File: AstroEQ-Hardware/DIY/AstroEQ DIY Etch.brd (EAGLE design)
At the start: 101.6 x 66 mm, 40 parts, among them IC1 ATMEGA162-16PU, IC2 PIC18F14K50-I/P, IC3 78L05, J1 POWER_JACKPTH, M1 POLOLU-CARRIER, M2 POLOLU-CARRIER, X1 16MHz, X2 12MHz

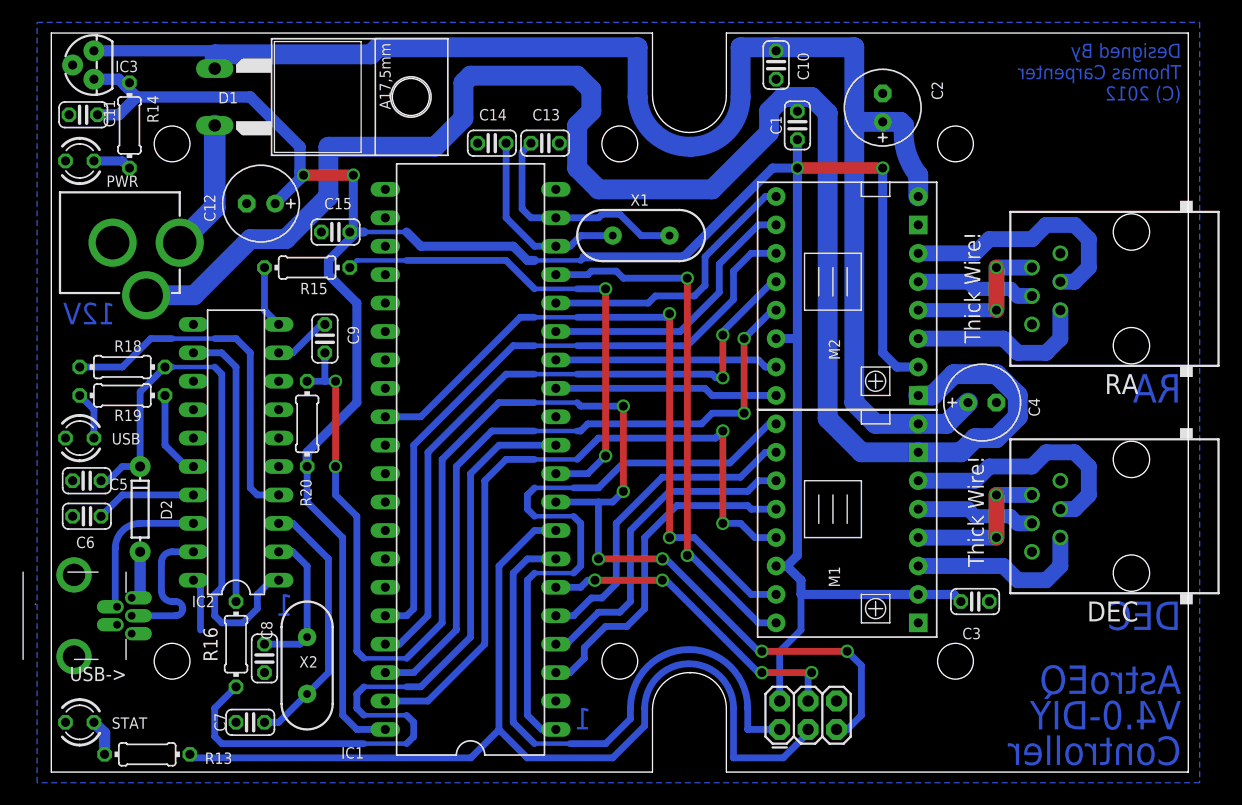
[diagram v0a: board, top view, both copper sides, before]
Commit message: Update DIY Eagle Designs
(1) Bring AstroEQ-DIY up to date (V4.4)
(2) Export AstroEQ-DIY schematic to PDF
(3) Make sure the etch file doesn't have holes in pads
(4) Add AstroEQ-ARD variant - Arduino Mega sheild
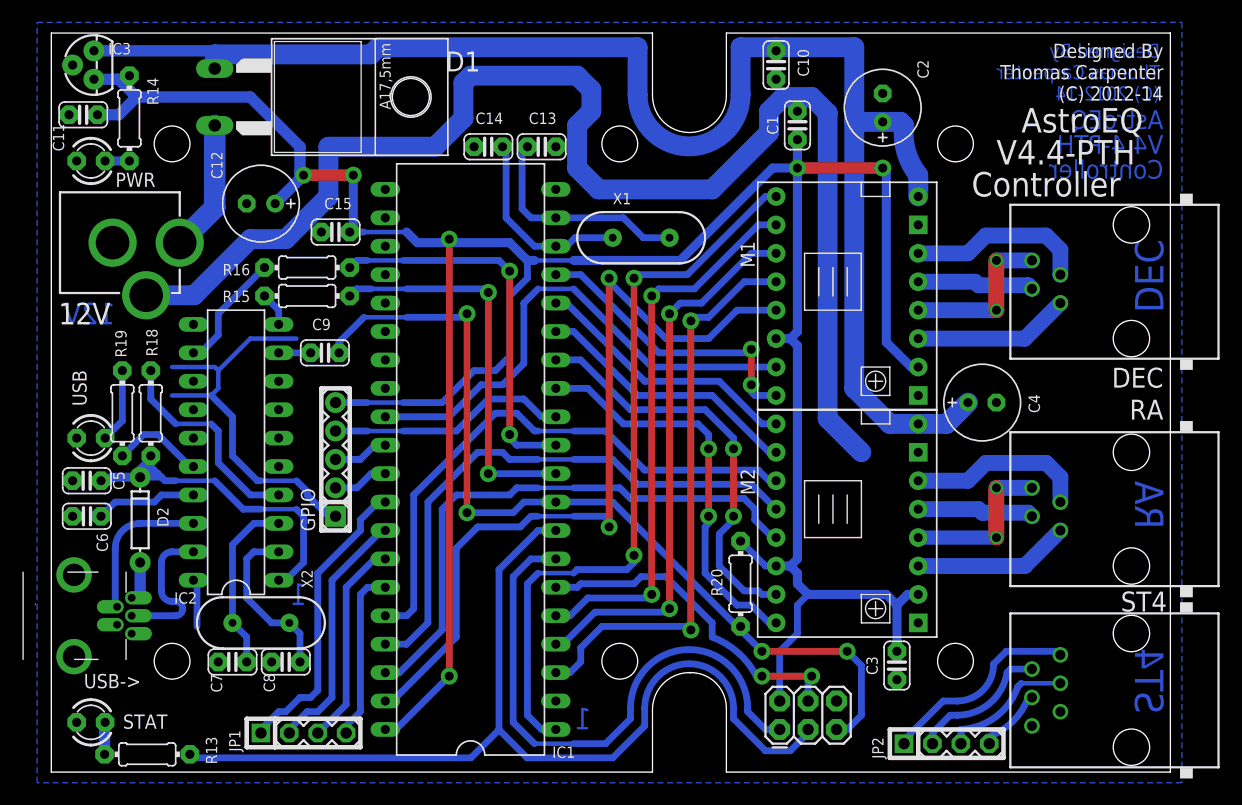
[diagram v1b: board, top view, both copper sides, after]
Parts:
- added GPIO: (no value), SparkFun:1X05
- added JP1, JP2: (no value), SparkFun:1X04
- added ST4: RJ11-6, con-tycoelectronics:RJ11-NO_SHIELD
- C13, C14, C6, C7, C8: device rcl:C025-024X044 -> resistor:C025-024X044
- DEC, RA: value RJ11-4X -> RJ11-4; device con-tycoelectronics:RJ11-NO_SHIELD -> con-tycoelectronics:RJ11-NO_SHIELD-4
- M1, M2: value POLOLU-CARRIER -> Motor Driver
- R15, R16: device SmartPrj:0204/7 -> rcl:0204/7
- moved R20 41.3 mm to (61.6, 16.8), turned to 90 degrees
- moved R16 34.2 mm to (22.9, 45.1), turned to 180 degrees
- moved DEC 21.0 mm to (96.5, 43.8)
- moved M1 20.3 mm to (71.1, 42.5)
- moved M2 20.3 mm to (71.1, 22.2)
- moved RA 19.7 mm to (96.5, 23.5)
- moved C3 9.03 mm to (75.6, 9.53), turned to 270 degrees
- moved C7 5.63 mm to (16.2, 9.84)
- moved X2 5.62 mm to (18.7, 13.3), turned to 180 degrees
- moved R18 4.85 mm to (8.89, 32.1), turned to 270 degrees
- moved R15 2.54 mm to (22.9, 42.5)
- moved C8 1.93 mm to (21.0, 9.84), turned to 180 degrees
- moved R19 1.59 mm to (6.35, 32.1), turned to 270 degrees
- moved C9 1.27 mm to (24.4, 37.5), turned to 0 degrees
- moved PWR 1.00 mm to (3.54, 54.6)
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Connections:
- new net DEC+: IC1.33, JP1.2
- new net DEC+B: JP2.2, ST4.5
- new net DEC-: IC1.34, JP1.3
- new net DEC-B: JP2.3, ST4.4
- new net IO0: GPIO.4, IC1.12
- new net IO1: GPIO.3, IC1.30
- new net IO2: GPIO.2, IC1.31
- new net RA+: IC1.32, JP1.1
- new net RA+B: JP2.1, ST4.6
- new net RA-: IC1.35, JP1.4
- new net RA-B: JP2.4, ST4.3
- net +5V: now also GPIO.5
- net GND: now also GPIO.1, ST4.2
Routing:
- net RESET: track 126.0 -> 80.3 mm, vias 8 -> 4
- net RX: track 67.2 -> 34.3 mm, vias 0 -> 2
- net RA+: track 0.00 -> 26.5 mm
- net +5V: track 235.9 -> 261.3 mm, vias 4 -> 6
- net DEC+: track 0.00 -> 22.4 mm
- net IO0: track 0.00 -> 21.5 mm
- net MS3-1: track 30.3 -> 51.3 mm, vias 0 -> 2
- net MS1-1: track 28.9 -> 49.8 mm, vias 0 -> 2
- net DIR-1: track 47.3 -> 26.7 mm
- net MS2-1: track 29.5 -> 49.6 mm, vias 0 -> 2
- net DEC-: track 0.00 -> 18.6 mm
- net RA+B: track 0.00 -> 17.7 mm
- net VPIC: track 49.3 -> 32.3 mm
- net STEP-2: track 19.9 -> 36.9 mm, vias 0 -> 2
- net DIR-2: track 19.9 -> 36.1 mm, vias 0 -> 2
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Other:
- board size 101.6 x 66 mm -> 100 x 66 mm
- board text added: "(C) 2012-14"
- board text added: "4988"
- board text added: "8824/5"
- board text added: "Markings show the location of the Potentiometers on the"
- board text added: "Pololu Boards depending on which chip they use."
- board text added: "ST4"
- board text added: "Sq Pad"
- board text added: "V4.4-PTH"
- board text removed: "(C) 2012"
- board text removed: "V4.0-DIY"

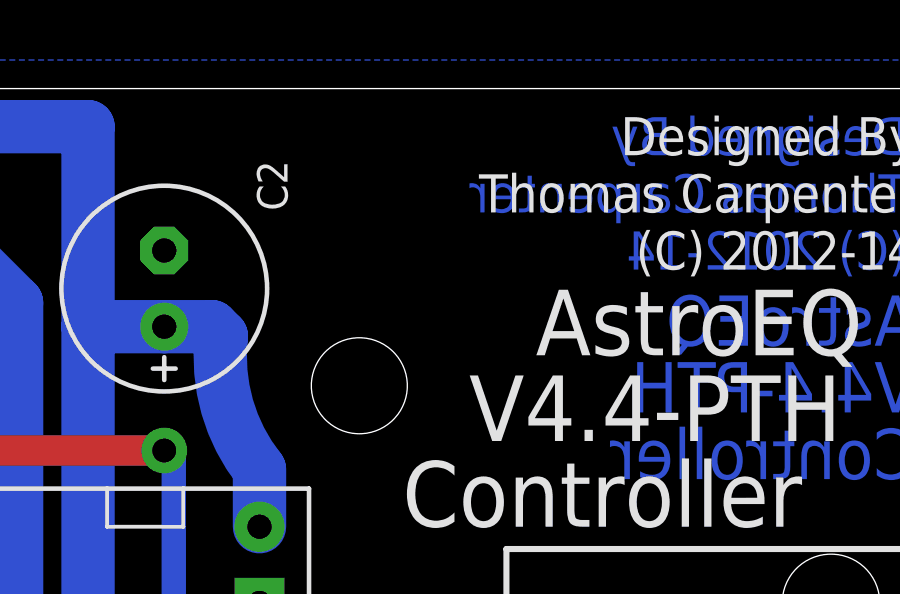
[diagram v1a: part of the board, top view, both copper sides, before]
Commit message: Update PCB Logo
Add AstroEQ logo to PCB hardware designs.
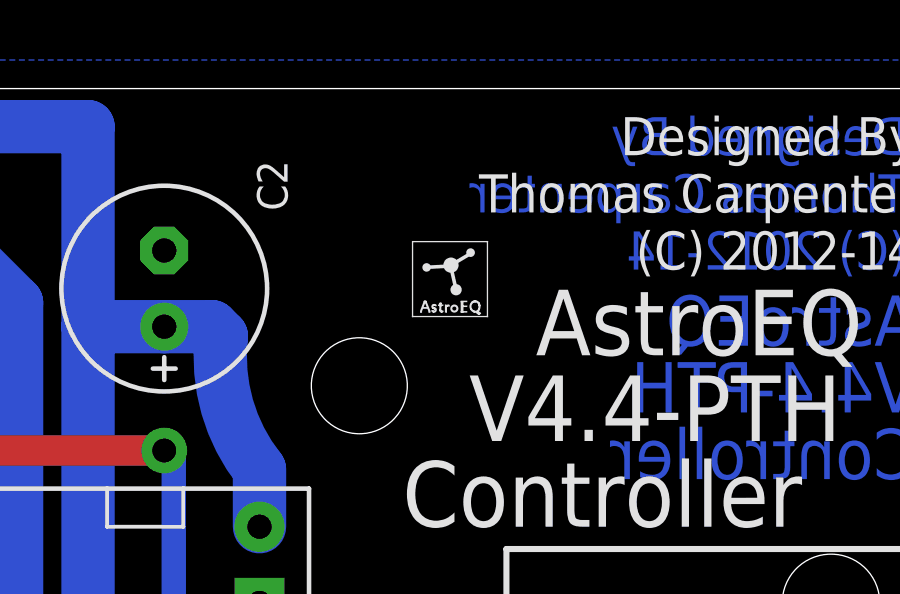
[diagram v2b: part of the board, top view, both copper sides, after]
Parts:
- added LOGO1: ASTROEQ3MM, CompanyLogos:ASTROEQ-MINI
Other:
- board text added: "Make sure to load the ground plane. Type 'ratsnest' and press enter."
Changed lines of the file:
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@@
 <layer number="17" name="Pads" color="2" fill="1" visible="yes" active="yes"/>
 <layer number="18" name="Vias" color="2" fill="1" visible="yes" active="yes"/>
-<layer number="19" name="Unrouted" color="6" fill="1" visible="no" active="yes"/>
+<layer number="19" name="Unrouted" color="6" fill="1" visible="yes" active="yes"/>
 <layer number="20" name="Dimension" color="15" fill="1" visible="yes" active="yes"/>
 <layer number="21" name="tPlace" color="7" fill="1" visible="no" active="yes"/>
@@
 <layer number="24" name="bOrigins" color="15" fill="1" visible="no" active="yes"/>
 <layer number="25" name="tNames" color="15" fill="1" visible="yes" active="yes"/>
-<layer number="26" name="bNames" color="7" fill="1" visible="yes" active="yes"/>
+<layer number="26" name="bNames" color="7" fill="1" visible="no" active="yes"/>
 <layer number="27" name="tValues" color="15" fill="1" visible="yes" active="yes"/>
-<layer number="28" name="bValues" color="7" fill="1" visible="yes" active="yes"/>
+<layer number="28" name="bValues" color="7" fill="1" visible="no" active="yes"/>
 <layer number="29" name="tStop" color="7" fill="3" visible="no" active="yes"/>
-<layer number="30" name="bStop" color="7" fill="6" visible="no" active="yes"/>
+<layer number="30" name="bStop" color="7" fill="6" visible="yes" active="yes"/>
 <layer number="31" name="tCream" color="7" fill="4" visible="no" active="yes"/>
 <layer number="32" name="bCream" color="7" fill="5" visible="no" active="yes"/>
@@
 <layer number="43" name="vRestrict" color="2" fill="10" visible="no" active="yes"/>
 <layer number="44" name="Drills" color="15" fill="1" visible="no" active="yes"/>
-<layer number="45" name="Holes" color="15" fill="1" visible="yes" active="yes"/>
+<layer number="45" name="Holes" color="15" fill="1" visible="no" active="yes"/>
 <layer number="46" name="Milling" color="3" fill="1" visible="no" active="yes"/>
 <layer number="47" name="Measures" color="7" fill="1" visible="no" active="yes"/>
-<layer number="48" name="Document" color="7" fill="1" visible="no" active="yes"/>
+<layer number="48" name="Document" color="7" fill="1" visible="yes" active="yes"/>
 <layer number="49" name="Reference" color="7" fill="1" visible="yes" active="yes"/>
 <layer number="50" name="dxf" color="7" fill="1" visible="no" active="no"/>
@@
 <layer number="110" name="fp0" color="7" fill="1" visible="no" active="yes"/>
 <layer number="111" name="LPC17xx" color="7" fill="1" visible="no" active="yes"/>
+<layer number="112" name="tSilk" color="7" fill="1" visible="no" active="yes"/>
 <layer number="116" name="Patch_BOT" color="9" fill="4" visible="no" active="yes"/>
 <layer number="121" name="_tsilk" color="7" fill="1" visible="no" active="yes"/>
@@
 <layer number="124" name="bTestmark" color="7" fill="1" visible="no" active="yes"/>
 <layer number="125" name="_tNames" color="7" fill="1" visible="no" active="yes"/>
+<layer number="126" name="_bNames" color="7" fill="1" visible="no" active="yes"/>
+<layer number="127" name="_tValues" color="7" fill="1" visible="no" active="yes"/>
+<layer number="128" name="_bValues" color="7" fill="1" visible="no" active="yes"/>
 <layer number="131" name="tAdjust" color="7" fill="1" visible="no" active="yes"/>
 <layer number="132" name="bAdjust" color="7" fill="1" visible="no" active="yes"/>
 <layer number="144" name="Drill_legend" color="7" fill="1" visible="no" active="yes"/>
 <layer number="151" name="HeatSink" color="7" fill="1" visible="no" active="yes"/>
+<layer number="152" name="_bDocu" color="7" fill="1" visible="no" active="yes"/>
 <layer number="199" name="Contour" color="7" fill="1" visible="no" active="yes"/>
 <layer number="200" name="200bmp" color="1" fill="10" visible="no" active="yes"/>
@@
 <layer number="223" name="223bmp" color="24" fill="1" visible="no" active="no"/>
 <layer number="224" name="224bmp" color="25" fill="1" visible="no" active="no"/>
+<layer number="248" name="Housing" color="7" fill="1" visible="no" active="yes"/>
+<layer number="249" name="Edge" color="7" fill="1" visible="no" active="yes"/>
 <layer number="250" name="Descript" color="3" fill="1" visible="no" active="no"/>
 <layer number="251" name="SMDround" color="12" fill="11" visible="no" active="no"/>
@@
 <text x="23.495" y="84.1375" size="1.778" layer="49">This board design is for those who choose to etch the board at home.</text>
 <text x="23.495" y="79.0575" size="1.778" layer="49">Use single-sided copper clad board. Preferably 1oz copper and 1.2mm thick (1.6mm acceptable)</text>
-<text x="23.495" y="71.4375" size="1.778" layer="49">When printing silkscreen on paper, only Tnames and Tvalues (and Dimension) layers should be visible.</text>
+<text x="23.495" y="68.8975" size="1.778" layer="49">When printing silkscreen on paper, only Tnames and Tvalues (and Dimension) layers should be visible.</text>
 <text x="-6.985" y="0.3175" size="1.778" layer="49" rot="R90">If using 1.6mm, area around USB connector needs to
 be thinned down to 1.2mm thick</text>
@@
 <text x="26.9875" y="54.61" size="1.016" layer="27" font="vector" ratio="15" align="center">Thick Wire!</text>
 <text x="22.86" y="14.9225" size="1.9304" layer="16" font="vector" ratio="20" rot="MR0">1</text>
+<text x="23.495" y="73.9775" size="1.778" layer="49">Make sure to load the ground plane. Type 'ratsnest' and press enter.</text>
 </plain>
 <attributes>
@@
 </element>
 <element name="GPIO" library="SparkFun" package="1X05" value="" x="25.4" y="22.86" rot="R90"/>
+<element name="LOGO1" library="CompanyLogos" package="ASTROEQ-MINI" value="ASTROEQ3MM" x="82.55" y="58.42"/>
 </elements>
 <signals>

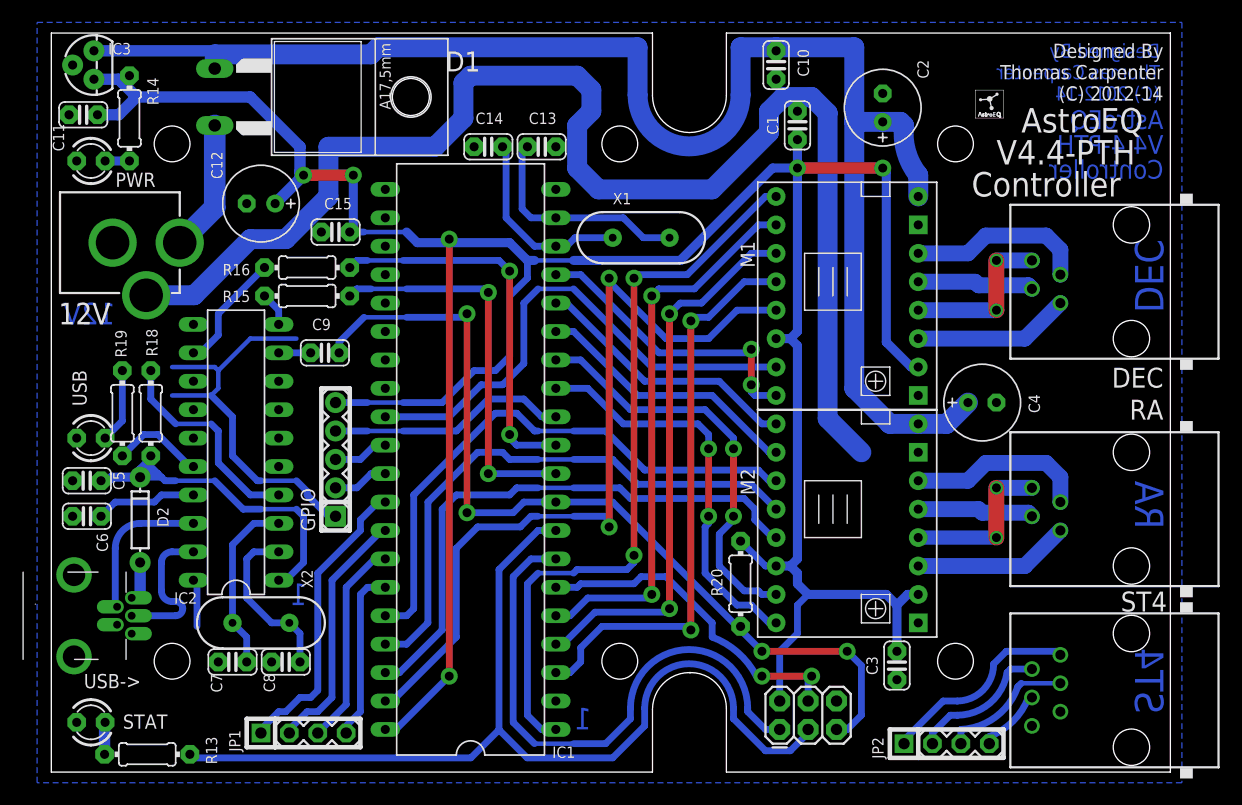
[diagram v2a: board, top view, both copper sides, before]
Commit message: Update AstroEQ DIY Design
The DIY version of the design (intended for home-etching on single-sided
PCB) was still V4.4. I have updated it to the V4.6 hardware.
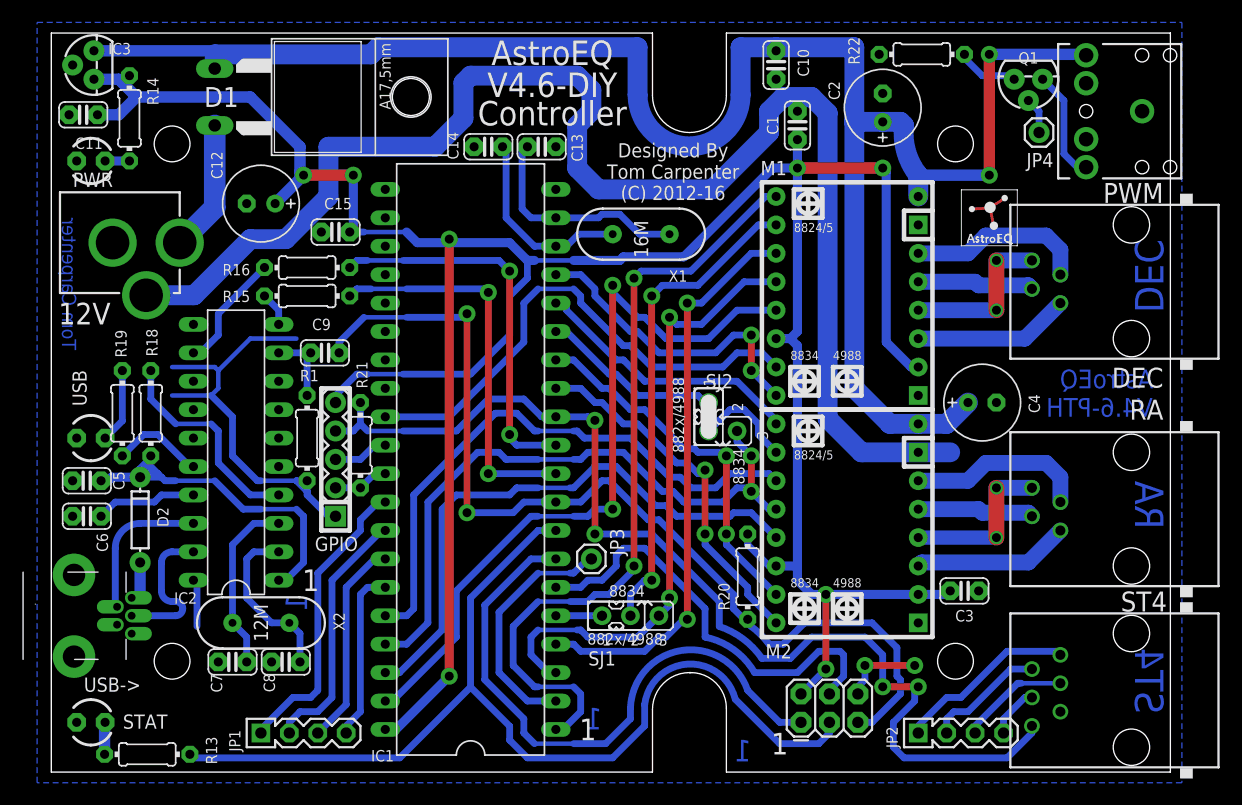
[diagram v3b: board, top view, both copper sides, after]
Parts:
- added J2, J3: (no value), jumper:JUMP
- added JP3, JP4: M01PTH, SparkFun:1X01
- added PWM: JACK, SparkFun:AUDIO-JACK
- added Q1: BS270, SparkFun:TO-92
- added R1: 10k, rcl:0204/7
- added R21: 1k, rcl:0204/7
- added R22: 120, rcl:0204/7
- added SJ1: (no value), jumper:JP2
- added SJ2: (no value), jumper:JP2L
- D1: value C3D06065A -> MBR1060
- HAMMOND-1593N: value HAMMOND-1593N -> HAMMOND-1593N-4HOLE; device holes:HAMMOND-1593N -> holes:HAMMOND-1593N4HOLES
- LOGO1: value ASTROEQ3MM -> ASTROEQ5MM; device CompanyLogos:ASTROEQ-MINI -> CompanyLogos:ASTROEQ-SMALL
- moved LOGO1 11.5 mm to (81.3, 47.0)
- moved C3 8.99 mm to (81.6, 16.2), turned to 0 degrees
- moved GPIO 5.08 mm to (25.4, 27.9)
- moved PROG 4.84 mm to (69.5, 5.71)
- moved JP2 1.59 mm to (77.5, 3.49)
- moved R20 0.90 mm to (62.2, 17.5)
- moved X1 0.32 mm to (52.7, 48.1)
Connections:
- removed net DEC+B: JP2.2, ST4.5
- removed net DEC-B: JP2.3, ST4.4
- removed net RA+B: JP2.1, ST4.6
- removed net RA-B: JP2.4, ST4.3
- new net DEC+/SI: IC1.33, JP1.2
- new net DEC-/CK: IC1.34, JP1.3
- new net MS13-1: M1.2, SJ1.2
- new net MS13-2: M2.2, SJ2.2
- new net PWM: IC1.2, JP3.1
- new net PWM-ILIM: Q1.3, R22.2
- new net PWM-OUT: PWM.RING, Q1.1
- new net PWM-Q1: JP4.1, Q1.2
- new net RA+/SO: IC1.32, JP1.1
- new net RA-/!SS: IC1.35, JP1.4
- net DEC+: now also JP2.2, ST4.5; no longer IC1.33, JP1.2
- net DEC-: now also JP2.3, ST4.4; no longer IC1.34, JP1.3
- net DTR: now also R1.1
- net GND: now also PWM.SLEEVE, R1.2, R22.1
- net IO0: now also R21.1, ST4.1
- net IO2: now also R21.2
- net MS1-1: now also SJ1.1; no longer M1.2
- net MS1-2: now also SJ2.1; no longer M2.2
- net MS3-1: now also SJ1.3
- net MS3-2: now also SJ2.3
- net RA+: now also JP2.1, ST4.6; no longer IC1.32, JP1.1
- net RA-: now also JP2.4, ST4.3; no longer IC1.35, JP1.4
- net V+: now also PWM.TIP
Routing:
- net IO0: track 21.5 -> 97.4 mm, vias 0 -> 4
- net MS1-1: track 49.8 -> 4.13 mm, vias 2 -> 0
- net MS13-1: track 0.00 -> 43.5 mm, vias 0 -> 2
- net RA+/SO: track 0.00 -> 26.5 mm
- net V+: track 133.1 -> 158.9 mm, vias 0 -> 2
- net DEC+/SI: track 0.00 -> 22.8 mm
- net PWM: track 0.00 -> 21.8 mm
- net DEC-/CK: track 0.00 -> 18.6 mm
- net RA+B: track 17.7 -> 0.00 mm
- net GND: track 160.8 -> 177.9 mm, vias 0 -> 2
- net RA-/!SS: track 0.00 -> 15.4 mm
- net DEC+B: track 12.0 -> 0.00 mm
- net DEC+: track 22.4 -> 10.7 mm
- net DEC-B: track 11.6 -> 0.00 mm
- net RA-: track 15.4 -> 4.60 mm
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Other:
- board text added: "(C) 2012-16"
- board text added: "12M"
- board text added: "16M"
- board text added: "882x/4988"
- board text added: "8834"
- board text added: "Tom Carpenter"
- board text added: "V4.6-DIY"
- board text added: "V4.6-PTH"
- board text removed: "(C) 2012-14"
- board text removed: "Sq Pad"
- board text removed: "Thick Wire!"
- board text removed: "Thomas Carpenter"
- board text removed: "V4.4-PTH"
